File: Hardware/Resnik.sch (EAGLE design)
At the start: 178 parts, among them IC1 ATMEGA644M, J1 CONN_82.54_SCREW, J3 CONN_82.54_SCREW, J4 CONN_42.54_SCREW, Q1 DMG3404, Q2 DMG3404, Q3 FDN360P, Q4 FDN360P, Q5 FDN360P, Q6 DMG3404, U1 TLV61220DBV, U10 SN74AUP1G04YFP, U11 SN74AUP2G86SOT833-1, U12 SN74AUP2G08DQE, U13 SN74AUP2G08DQE, U14 SN74AUP2G08DQE, U15 MIC2039MT, U16 MIC2039MT, U17 MIC2039MT, U18 MIC2039MT, U19 TPS22917DBV, U2 TPS62822DLC, U20 TPS22917DBV, U21 TXS0102DQM, U22 BME280, U23 FT231X-Q, U24 TPS22917DBV, U25 TXS0108RGY, U26 TXS0108RGY, U27 TXS0104RGY, U28 MCP4726A2SOT-23, U29 ADS1115, U3 TPS61032RSA, U30 ADS1115, U31 INA211DCK, U32 INA210DCK, U33 TCA9555RTW, U5 BQ2980RUG, U6 TPS2105, U7 LTC4412S6, U8 TPS79733, U9 SN74AUP1G04YFP

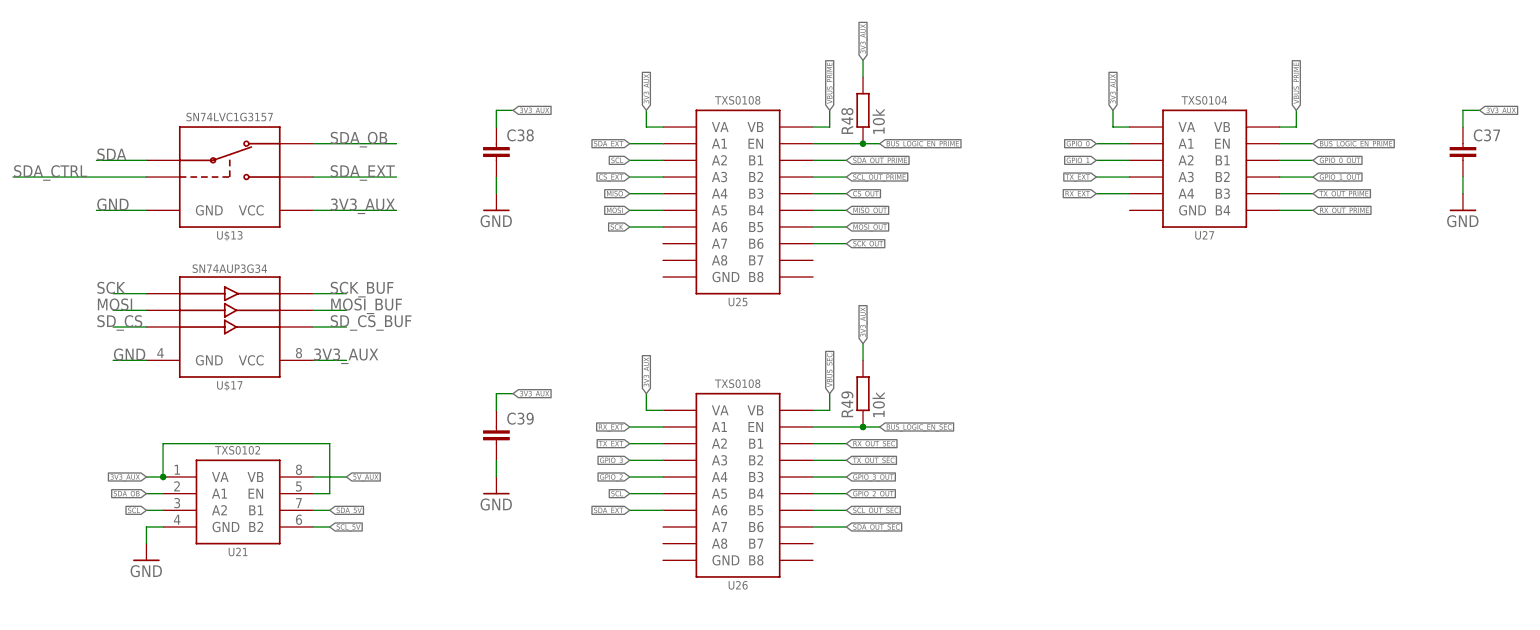
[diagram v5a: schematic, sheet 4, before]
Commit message: Continued layout, starting on SD and Feather header
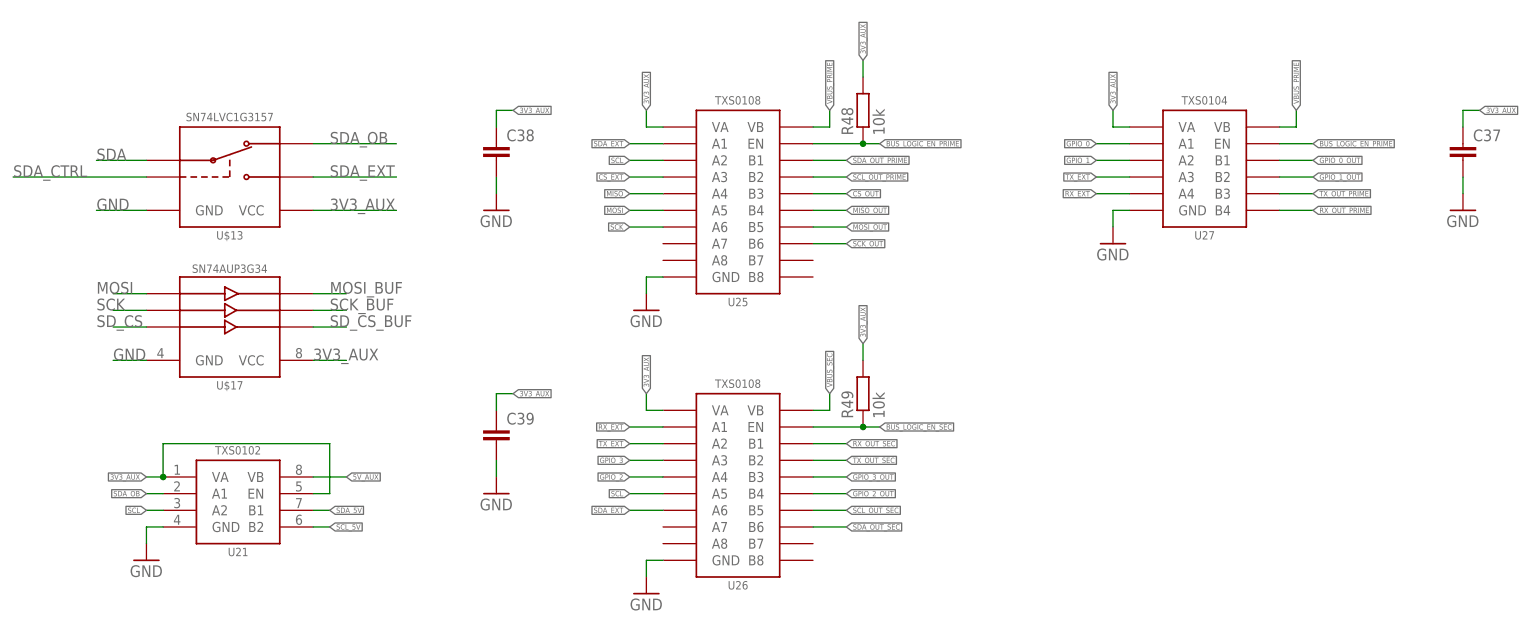
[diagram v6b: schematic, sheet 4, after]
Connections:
- net GND: now also U25.GND, U26.GND, U27.GND
- net MOSI: now also U$17.1A; no longer U$17.2A
- net MOSI_BUF: now also U$17.1Y; no longer U$17.2Y
- net SCK: now also U$17.2A; no longer U$17.1A
- net SCK_BUF: now also U$17.2Y; no longer U$17.1Y
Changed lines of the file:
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@@
 <part name="H2" library="bschulz" deviceset="MOUNTING_HOLE" device="4_NP"/>
 <part name="H3" library="bschulz" deviceset="MOUNTING_HOLE" device="4_NP"/>
+<part name="GND68" library="supply1" library_urn="urn:adsk.eagle:library:371" deviceset="GND" device=""/>
+<part name="GND69" library="supply1" library_urn="urn:adsk.eagle:library:371" deviceset="GND" device=""/>
+<part name="GND70" library="supply1" library_urn="urn:adsk.eagle:library:371" deviceset="GND" device=""/>
 </parts>
 <sheets>
@@
 <instance part="C39" gate="G$1" x="63.5" y="40.64"/>
 <instance part="GND67" gate="1" x="63.5" y="30.48"/>
+<instance part="GND68" gate="1" x="86.36" y="58.42"/>
+<instance part="GND69" gate="1" x="86.36" y="15.24"/>
+<instance part="GND70" gate="1" x="157.48" y="68.58"/>
 </instances>
 <busses>
@@
 <wire x1="63.5" y1="35.56" x2="63.5" y2="33.02" width="0.1524" layer="91"/>
 <pinref part="GND67" gate="1" pin="GND"/>
+</segment>
+<segment>
+<pinref part="U25" gate="G$1" pin="GND"/>
+<wire x1="88.9" y1="63.5" x2="86.36" y2="63.5" width="0.1524" layer="91"/>
+<wire x1="86.36" y1="63.5" x2="86.36" y2="60.96" width="0.1524" layer="91"/>
+<pinref part="GND68" gate="1" pin="GND"/>
+</segment>
+<segment>
+<pinref part="U26" gate="G$1" pin="GND"/>
+<wire x1="88.9" y1="20.32" x2="86.36" y2="20.32" width="0.1524" layer="91"/>
+<wire x1="86.36" y1="20.32" x2="86.36" y2="17.78" width="0.1524" layer="91"/>
+<pinref part="GND69" gate="1" pin="GND"/>
+</segment>
+<segment>
+<pinref part="U27" gate="G$1" pin="GND"/>
+<wire x1="160.02" y1="73.66" x2="157.48" y2="73.66" width="0.1524" layer="91"/>
+<wire x1="157.48" y1="73.66" x2="157.48" y2="71.12" width="0.1524" layer="91"/>
+<pinref part="GND70" gate="1" pin="GND"/>
 </segment>
 </net>
@@
 <net name="MOSI" class="0">
 <segment>
+<wire x1="88.9" y1="73.66" x2="83.82" y2="73.66" width="0.1524" layer="91"/>
+<label x="83.82" y="73.66" size="0.8128" layer="95" rot="R180" xref="yes"/>
+<pinref part="U25" gate="G$1" pin="A5"/>
+</segment>
+<segment>
+<pinref part="U$17" gate="G$1" pin="1A"/>
+<wire x1="10.16" y1="60.96" x2="5.08" y2="60.96" width="0.1524" layer="91"/>
+<label x="2.54" y="60.96" size="1.778" layer="95"/>
+</segment>
+</net>
+<net name="SCK" class="0">
+<segment>
+<wire x1="88.9" y1="71.12" x2="83.82" y2="71.12" width="0.1524" layer="91"/>
+<label x="83.82" y="71.12" size="0.8128" layer="95" rot="R180" xref="yes"/>
+<pinref part="U25" gate="G$1" pin="A6"/>
+</segment>
+<segment>
 <pinref part="U$17" gate="G$1" pin="2A"/>
 <wire x1="10.16" y1="58.42" x2="5.08" y2="58.42" width="0.1524" layer="91"/>
 <label x="2.54" y="58.42" size="1.778" layer="95"/>
 </segment>
-<segment>
-<wire x1="88.9" y1="73.66" x2="83.82" y2="73.66" width="0.1524" layer="91"/>
-<label x="83.82" y="73.66" size="0.8128" layer="95" rot="R180" xref="yes"/>
-<pinref part="U25" gate="G$1" pin="A5"/>
-</segment>
-</net>
-<net name="SCK" class="0">
-<segment>
-<pinref part="U$17" gate="G$1" pin="1A"/>
-<wire x1="10.16" y1="60.96" x2="5.08" y2="60.96" width="0.1524" layer="91"/>
-<label x="2.54" y="60.96" size="1.778" layer="95"/>
-</segment>
-<segment>
-<wire x1="88.9" y1="71.12" x2="83.82" y2="71.12" width="0.1524" layer="91"/>
-<label x="83.82" y="71.12" size="0.8128" layer="95" rot="R180" xref="yes"/>
-<pinref part="U25" gate="G$1" pin="A6"/>
-</segment>
 </net>
 <net name="SD_CS" class="0">
@@
 </segment>
 </net>
-<net name="MOSI_BUF" class="0">
+<net name="SCK_BUF" class="0">
 <segment>
 <pinref part="U$17" gate="G$1" pin="2Y"/>
 <wire x1="35.56" y1="58.42" x2="40.64" y2="58.42" width="0.1524" layer="91"/>
 <label x="38.1" y="58.42" size="1.778" layer="95"/>
-</segment>
-</net>
-<net name="SCK_BUF" class="0">
-<segment>
-<pinref part="U$17" gate="G$1" pin="1Y"/>
-<wire x1="35.56" y1="60.96" x2="40.64" y2="60.96" width="0.1524" layer="91"/>
-<label x="38.1" y="60.96" size="1.778" layer="95"/>
 </segment>
 </net>
@@
 </segment>
 </net>
+<net name="MOSI_BUF" class="0">
+<segment>
+<pinref part="U$17" gate="G$1" pin="1Y"/>
+<wire x1="35.56" y1="60.96" x2="40.64" y2="60.96" width="0.1524" layer="91"/>
+<label x="38.1" y="60.96" size="1.778" layer="95"/>
+</segment>
+</net>

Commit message: Layout tentative completed, sent to DFM check
Layout complete for v0.0, pending final triple check, sent to DFM check to verify manufacture issues. Ready for final external review.
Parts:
- removed H1: (no value), bschulz:MOUNTING_HOLE4_NP
- added H4: (no value), bschulz:MOUNTING_HOLE4_NP
- added R6: 10k, bschulz_passives:R-EU_R0402
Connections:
- removed net V_BETA_CTL: U7.CTL
- new net V_HP_SYNC: U3.SYNC, U33.P12
- net 3V3_CORE: now also R6.2
- net BUS_LOGIC_EN_SEC: now also U33.P10
- net FAULT_SEC: now also U33.P16
- net FEATHER_EN: now also U33.P17
- net GLOBAL_INT: now also R6.1
- net GND: now also J1.1, J4.1, U7.CTL; no longer J1.2, J4.2, U3.SYNC
- net PG_LDO: now also U33.P11; no longer U33.P10
- net VBUS_PRIME: now also J1.2; no longer J1.1
- net VBUS_SEC: now also J4.2; no longer J4.1
- net VUSB_POWER: now also Q3.D; no longer Q4.D
- net V_LI: now also Q4.D; no longer Q3.D
- net WD_DONE: now also MS1.GPIOA3
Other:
- note added: "ADD: --MPPT, CHRG (Input) --MPPT, FAULT (Input) --MPPT, SHDN (Output) --Feather PowerOn (Output) --ADC, OnBoard, Alert/RDY (Input, Interrupt) --ADC, OffBoard, Alert/RDY (Input, Interrupt) --Vusb (Input) --LevelShifter, Primary Bus, EN (Output) --LevelShifter, Secondary Bus, EN (Output) --BMS, CTR (Output) --BusPowerSwitch, Primary Bus, Fault (Input) --BusPowerSwitch, Secondary Bus, Fault (Input) 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"
- note added: "Global Int Pullup!"
- note added: "Remove LBI pullup??"
- note added: "Remove PG pullup?"
- note added: "VBETA CONTROL!!!!!!!!!!!"
- note removed: "ADD: --MPPT, CHRG (Input) --MPPT, FAULT (Input) --MPPT, SHDN (Output) Feather PowerOn (Output) --ADC, OnBoard, Alert/RDY (Input, Interrupt) --ADC, OffBoard, Alert/RDY (Input, Interrupt) --Vusb (Input) --LevelShifter, Primary Bus, EN (Output) LevelShifter, Secondary Bus, EN (Output) --BMS, CTR (Output) --BusPowerSwitch, Primary Bus, Fault (Input) BusPowerSwitch, Secondary Bus, Fault (Input) --High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"

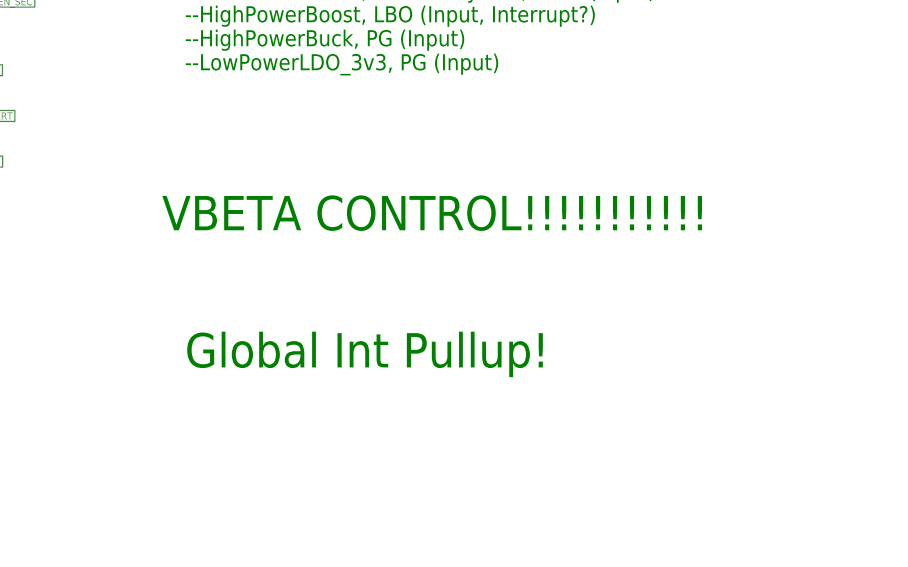
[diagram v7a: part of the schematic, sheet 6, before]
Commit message: Added PDFs of prelim v0.0 schematic
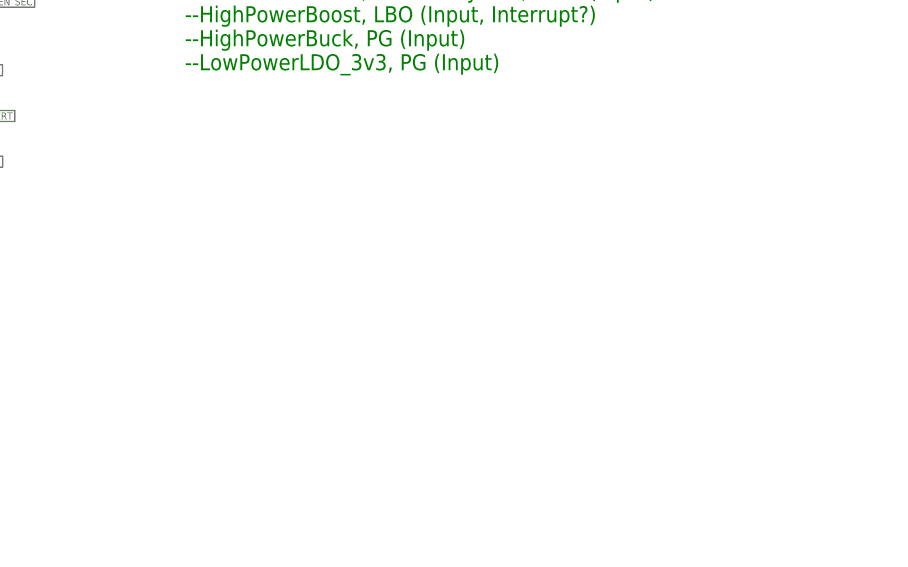
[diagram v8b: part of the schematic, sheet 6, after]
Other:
- note removed: "Global Int Pullup!"
- note removed: "VBETA CONTROL!!!!!!!!!!!"
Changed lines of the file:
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@@
 --HighPowerBuck, PG (Input)
 --LowPowerLDO_3v3, PG (Input)</text>
-<text x="213.36" y="58.42" size="3.81" layer="91">VBETA CONTROL!!!!!!!!!!!</text>
-<text x="215.9" y="43.18" size="3.81" layer="91">Global Int Pullup!</text>
 </plain>
 <instances>
